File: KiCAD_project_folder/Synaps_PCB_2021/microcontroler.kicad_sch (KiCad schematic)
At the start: 9 parts, among them U2 ESP32-WROOM-32

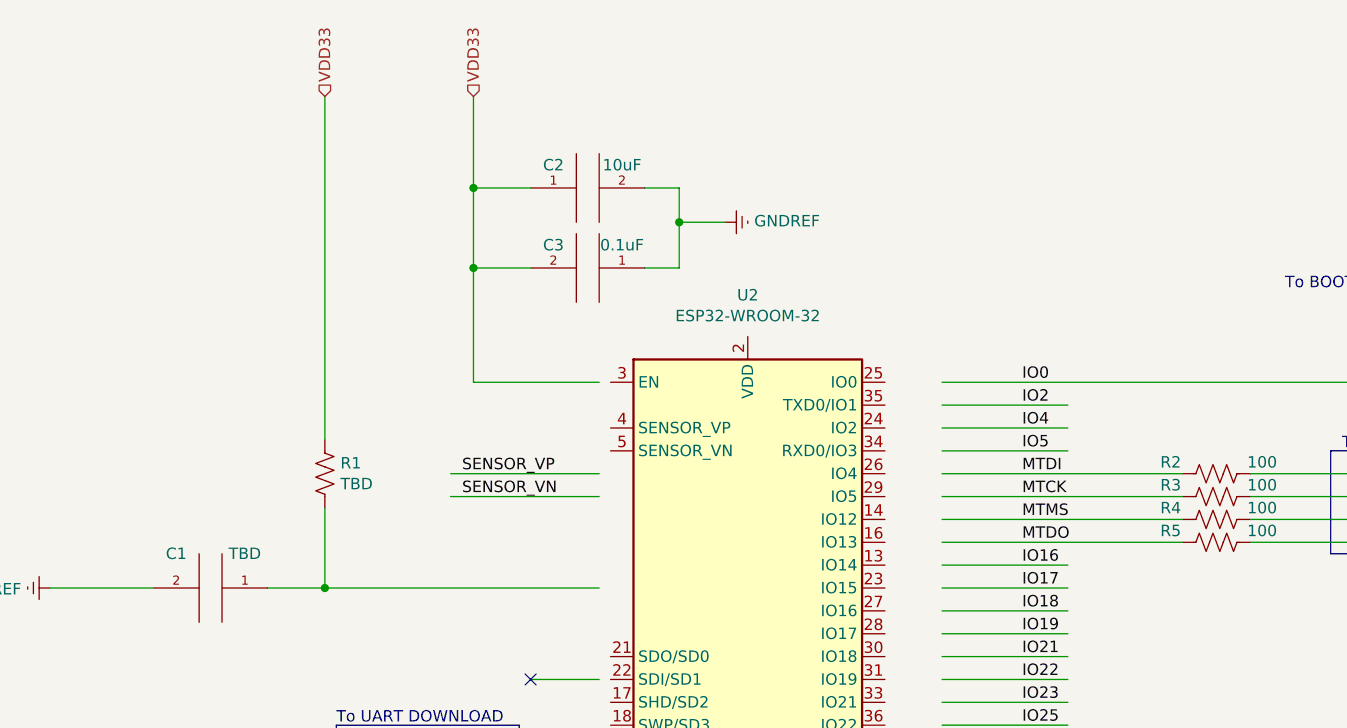
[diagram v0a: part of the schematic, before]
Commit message: Added library for one piece
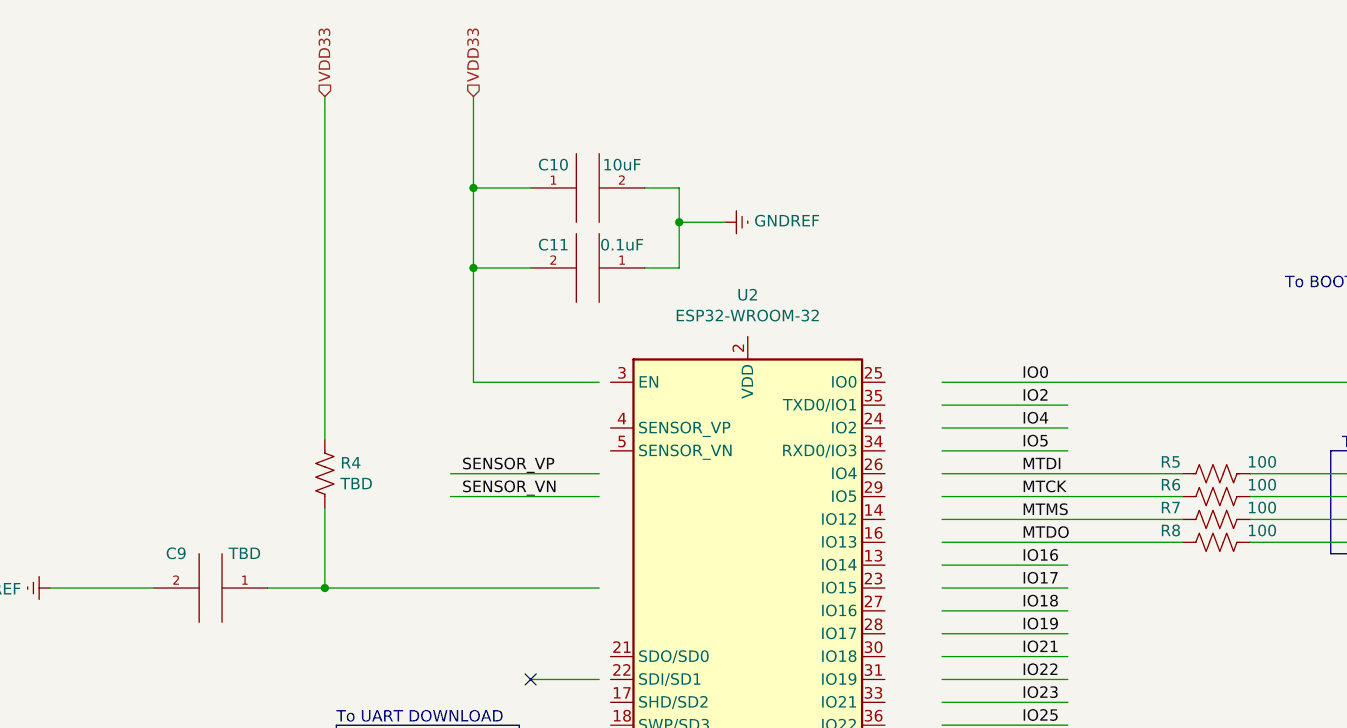
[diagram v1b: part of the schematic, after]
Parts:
- renumbered C2 to C10, C3 to C11, C1 to C9, R1 to R4, R2 to R5, R3 to R6, R4 to R7, R5 to R8
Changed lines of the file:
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@@
   (symbol (lib_id "power:GNDREF") (at 173.99 128.27 0) (unit 1)
     (in_bom yes) (on_board yes)
-    (property "Reference" "#PWR03" (id 0) (at 173.99 134.62 0)
+    (property "Reference" "#PWR013" (id 0) (at 173.99 134.62 0)
       (effects (font (size 1.27 1.27)) hide)
     )
@@
   (symbol (lib_id "power:GNDREF") (at 175.26 119.38 90) (unit 1)
     (in_bom yes) (on_board yes)
-    (property "Reference" "#PWR04" (id 0) (at 181.61 119.38 0)
+    (property "Reference" "#PWR014" (id 0) (at 181.61 119.38 0)
       (effects (font (size 1.27 1.27)) hide)
     )
@@
   (symbol (lib_id "pspice:CAP") (at 127 36.83 90) (unit 1)
     (in_bom yes) (on_board yes)
-    (property "Reference" "C2" (id 0) (at 123.19 34.29 90))
+    (property "Reference" "C10" (id 0) (at 123.19 34.29 90))
     (property "Value" "10uF" (id 1) (at 130.81 34.29 90))
     (property "Footprint" "" (id 2) (at 127 36.83 0)
@@
   (symbol (lib_id "pspice:CAP") (at 127 45.72 270) (unit 1)
     (in_bom yes) (on_board yes)
-    (property "Reference" "C3" (id 0) (at 123.19 43.18 90))
+    (property "Reference" "C11" (id 0) (at 123.19 43.18 90))
     (property "Value" "0.1uF" (id 1) (at 130.81 43.18 90))
     (property "Footprint" "" (id 2) (at 127 45.72 0)
@@
   (symbol (lib_id "Device:R_US") (at 97.79 68.58 0) (unit 1)
     (in_bom yes) (on_board yes)
-    (property "Reference" "R1" (id 0) (at 99.5172 67.4116 0)
+    (property "Reference" "R4" (id 0) (at 99.5172 67.4116 0)
       (effects (font (size 1.27 1.27)) (justify left))
     )
@@
   (symbol (lib_id "pspice:CAP") (at 85.09 81.28 270) (unit 1)
     (in_bom yes) (on_board yes)
-    (property "Reference" "C1" (id 0) (at 81.28 77.47 90))
+    (property "Reference" "C9" (id 0) (at 81.28 77.47 90))
     (property "Value" "TBD" (id 1) (at 88.9 77.47 90))
     (property "Footprint" "" (id 2) (at 85.09 81.28 0)
@@
   (symbol (lib_id "power:GNDREF") (at 67.31 81.28 270) (unit 1)
     (in_bom yes) (on_board yes)
-    (property "Reference" "#PWR01" (id 0) (at 60.96 81.28 0)
+    (property "Reference" "#PWR011" (id 0) (at 60.96 81.28 0)
       (effects (font (size 1.27 1.27)) hide)
     )
@@
   (symbol (lib_id "power:GNDREF") (at 190.5 120.65 0) (unit 1)
     (in_bom yes) (on_board yes)
-    (property "Reference" "#PWR05" (id 0) (at 190.5 127 0)
+    (property "Reference" "#PWR015" (id 0) (at 190.5 127 0)
       (effects (font (size 1.27 1.27)) hide)
     )
@@
   (symbol (lib_id "power:GNDREF") (at 142.24 40.64 90) (unit 1)
     (in_bom yes) (on_board yes)
-    (property "Reference" "#PWR02" (id 0) (at 148.59 40.64 0)
+    (property "Reference" "#PWR012" (id 0) (at 148.59 40.64 0)
       (effects (font (size 1.27 1.27)) hide)
     )
@@
   (symbol (lib_id "Device:R_US") (at 196.85 68.58 270) (unit 1)
     (in_bom yes) (on_board yes)
-    (property "Reference" "R2" (id 0) (at 191.77 67.31 90))
+    (property "Reference" "R5" (id 0) (at 191.77 67.31 90))
     (property "Value" "100" (id 1) (at 201.93 67.31 90))
     (property "Footprint" "" (id 2) (at 196.596 69.596 90)
@@
   (symbol (lib_id "Device:R_US") (at 196.85 73.66 270) (unit 1)
     (in_bom yes) (on_board yes)
-    (property "Reference" "R4" (id 0) (at 191.77 72.39 90))
+    (property "Reference" "R7" (id 0) (at 191.77 72.39 90))
     (property "Value" "100" (id 1) (at 201.93 72.39 90))
     (property "Footprint" "" (id 2) (at 196.596 74.676 90)
@@
   (symbol (lib_id "Device:R_US") (at 196.85 71.12 270) (unit 1)
     (in_bom yes) (on_board yes)
-    (property "Reference" "R3" (id 0) (at 191.77 69.85 90))
+    (property "Reference" "R6" (id 0) (at 191.77 69.85 90))
     (property "Value" "100" (id 1) (at 201.93 69.85 90))
     (property "Footprint" "" (id 2) (at 196.596 72.136 90)
@@
   (symbol (lib_id "Device:R_US") (at 196.85 76.2 270) (unit 1)
     (in_bom yes) (on_board yes)
-    (property "Reference" "R5" (id 0) (at 191.77 74.93 90))
+    (property "Reference" "R8" (id 0) (at 191.77 74.93 90))
     (property "Value" "100" (id 1) (at 201.93 74.93 90))
     (property "Footprint" "" (id 2) (at 196.596 77.216 90)

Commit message: Added basic PCB guidelines
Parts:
- C10, C11, C9: footprint (none) -> Capacitor_SMD:C_1206_3216Metric_Pad1.33x1.80mm_HandSolder
- R4, R5, R6, R7, R8: footprint (none) -> Resistor_SMD:R_1206_3216Metric_Pad1.30x1.75mm_HandSolder
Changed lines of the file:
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@@
     (property "Reference" "C10" (id 0) (at 123.19 34.29 90))
     (property "Value" "10uF" (id 1) (at 130.81 34.29 90))
-    (property "Footprint" "" (id 2) (at 127 36.83 0)
+    (property "Footprint" "Capacitor_SMD:C_1206_3216Metric_Pad1.33x1.80mm_HandSolder" (id 2) (at 127 36.83 0)
       (effects (font (size 1.27 1.27)) hide)
     )
@@
     (property "Reference" "C11" (id 0) (at 123.19 43.18 90))
     (property "Value" "0.1uF" (id 1) (at 130.81 43.18 90))
-    (property "Footprint" "" (id 2) (at 127 45.72 0)
+    (property "Footprint" "Capacitor_SMD:C_1206_3216Metric_Pad1.33x1.80mm_HandSolder" (id 2) (at 127 45.72 0)
       (effects (font (size 1.27 1.27)) hide)
     )
@@
       (effects (font (size 1.27 1.27)) (justify left))
     )
-    (property "Footprint" "" (id 2) (at 98.806 68.834 90)
+    (property "Footprint" "Resistor_SMD:R_1206_3216Metric_Pad1.30x1.75mm_HandSolder" (id 2) (at 98.806 68.834 90)
       (effects (font (size 1.27 1.27)) hide)
     )
@@
     (property "Reference" "C9" (id 0) (at 81.28 77.47 90))
     (property "Value" "TBD" (id 1) (at 88.9 77.47 90))
-    (property "Footprint" "" (id 2) (at 85.09 81.28 0)
+    (property "Footprint" "Capacitor_SMD:C_1206_3216Metric_Pad1.33x1.80mm_HandSolder" (id 2) (at 85.09 81.28 0)
       (effects (font (size 1.27 1.27)) hide)
     )
@@
     (property "Reference" "R5" (id 0) (at 191.77 67.31 90))
     (property "Value" "100" (id 1) (at 201.93 67.31 90))
-    (property "Footprint" "" (id 2) (at 196.596 69.596 90)
+    (property "Footprint" "Resistor_SMD:R_1206_3216Metric_Pad1.30x1.75mm_HandSolder" (id 2) (at 196.596 69.596 90)
       (effects (font (size 1.27 1.27)) hide)
     )
@@
     (property "Reference" "R7" (id 0) (at 191.77 72.39 90))
     (property "Value" "100" (id 1) (at 201.93 72.39 90))
-    (property "Footprint" "" (id 2) (at 196.596 74.676 90)
+    (property "Footprint" "Resistor_SMD:R_1206_3216Metric_Pad1.30x1.75mm_HandSolder" (id 2) (at 196.596 74.676 90)
       (effects (font (size 1.27 1.27)) hide)
     )
@@
     (property "Reference" "R6" (id 0) (at 191.77 69.85 90))
     (property "Value" "100" (id 1) (at 201.93 69.85 90))
-    (property "Footprint" "" (id 2) (at 196.596 72.136 90)
+    (property "Footprint" "Resistor_SMD:R_1206_3216Metric_Pad1.30x1.75mm_HandSolder" (id 2) (at 196.596 72.136 90)
       (effects (font (size 1.27 1.27)) hide)
     )
@@
     (property "Reference" "R8" (id 0) (at 191.77 74.93 90))
     (property "Value" "100" (id 1) (at 201.93 74.93 90))
-    (property "Footprint" "" (id 2) (at 196.596 77.216 90)
+    (property "Footprint" "Resistor_SMD:R_1206_3216Metric_Pad1.30x1.75mm_HandSolder" (id 2) (at 196.596 77.216 90)
       (effects (font (size 1.27 1.27)) hide)
     )

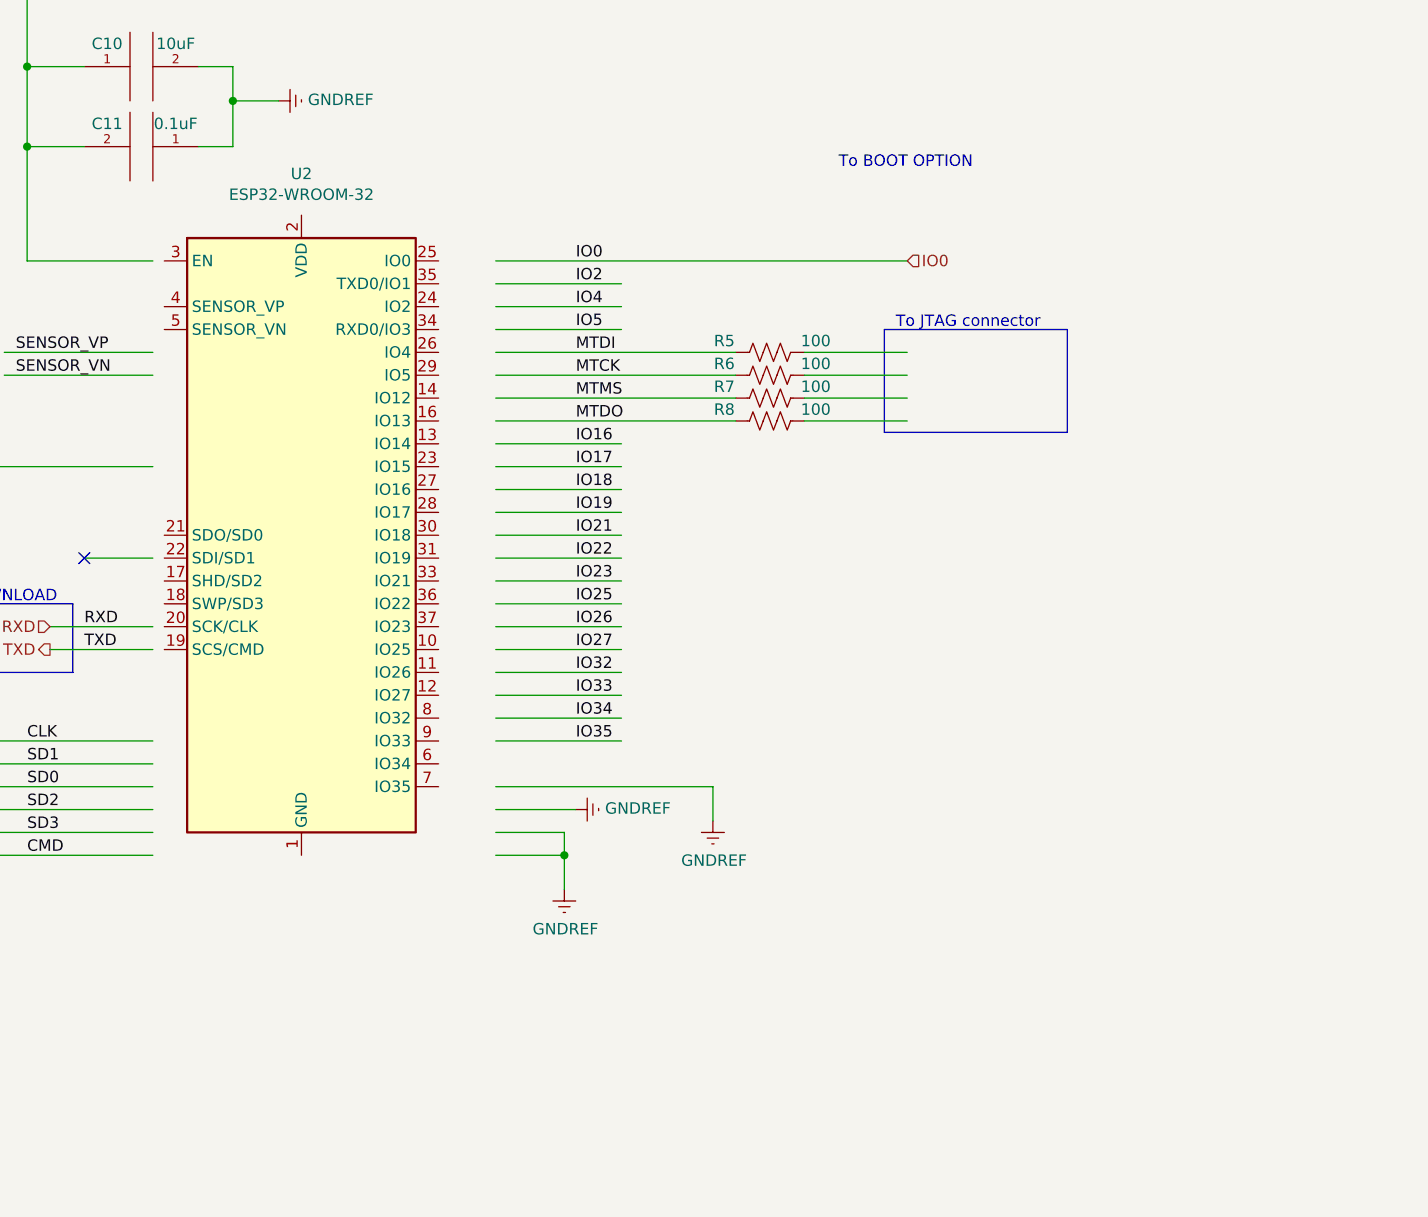
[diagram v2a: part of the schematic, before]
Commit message: Added new ESP32-S2 model
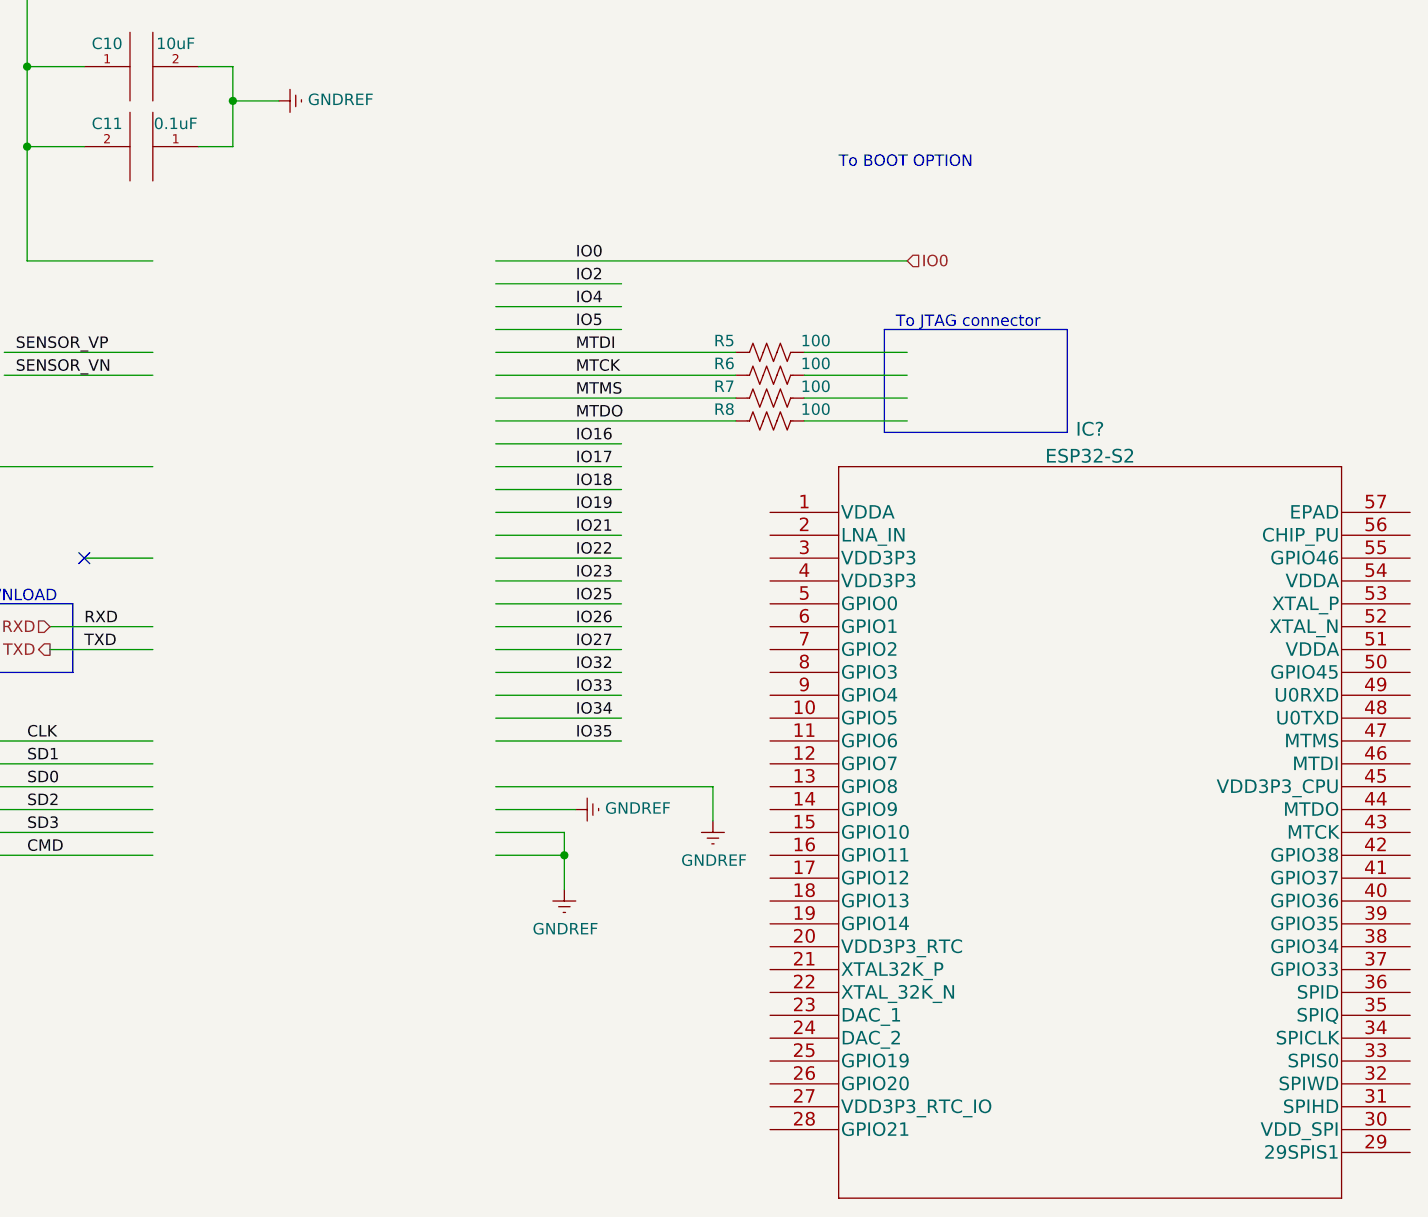
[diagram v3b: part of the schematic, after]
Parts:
- removed U2: ESP32-WROOM-32, RF_Module:ESP32-WROOM-32, symbol RF_Module:ESP32-WROOM-32
- added IC?: ESP32-S2, QFN56_ESP32_7X7_EXP, symbol ESP32-S2:ESP32-S2
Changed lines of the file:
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@@
     (pin "2")
   )
-  (symbol (lib_id "RF_Module:ESP32-WROOM-32") (at 144.78 88.9 0) (unit 1)
-    (in_bom yes) (on_board yes)
-    (property "Reference" "U2" (id 0) (at 144.78 48.7426 0))
-    (property "Value" "ESP32-WROOM-32" (id 1) (at 144.78 51.054 0))
-    (property "Footprint" "RF_Module:ESP32-WROOM-32" (id 2) (at 144.78 127 0)
-      (effects (font (size 1.27 1.27)) hide)
+  (symbol (lib_id "ESP32-S2:ESP32-S2") (at 196.85 86.36 0) (unit 1)
+    (in_bom yes) (on_board yes) (fields_autoplaced)
+    (property "Reference" "IC?" (id 0) (at 232.41 77.1324 0)
+      (effects (font (size 1.524 1.524)))
     )
-    (property "Datasheet" "https://www.espressif.com/sites/default/files/documentation/esp32-wroom-32_datasheet_en.pdf" (id 3) (at 137.16 87.63 0)
-      (effects (font (size 1.27 1.27)) hide)
+    (property "Value" "ESP32-S2" (id 1) (at 232.41 80.1258 0)
+      (effects (font (size 1.524 1.524)))
+    )
+    (property "Footprint" "QFN56_ESP32_7X7_EXP" (id 2) (at 232.41 80.264 0)
+      (effects (font (size 1.524 1.524)) hide)
+    )
+    (property "Datasheet" "" (id 3) (at 196.85 86.36 0)
+      (effects (font (size 1.524 1.524)))
     )
     (pin "1")
@@
     (pin "39")
     (pin "4")
+    (pin "40")
+    (pin "41")
+    (pin "42")
+    (pin "43")
+    (pin "44")
+    (pin "45")
+    (pin "46")
+    (pin "47")
+    (pin "48")
+    (pin "49")
     (pin "5")
+    (pin "50")
+    (pin "51")
+    (pin "52")
+    (pin "53")
+    (pin "54")
+    (pin "55")
+    (pin "56")
+    (pin "57")
     (pin "6")
     (pin "7")
